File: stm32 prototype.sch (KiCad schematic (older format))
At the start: 98 parts, among them J1 Conn_01x04, J10 Conn_01x03, J12 Conn_01x07, J13 Conn_01x06, J2 Conn_02x05_Odd_Even, J3 Conn_01x08, J4 Conn_01x06, J5 Conn_01x06, J6 Conn_01x06, J7 Conn_01x06, J8 Conn_ARM_JTAG_SWD_10, J9 Conn_01x03, Q1 Q_NMOS_GSD, Q2 Q_NMOS_GSD, Q3 Q_NMOS_GSD, Q4 Q_NMOS_GSD, Q5 Q_NMOS_GSD, Q6 Q_NMOS_GSD, Q7 Q_NMOS_GSD, Q8 Q_NMOS_GSD, SW1 SW_Push, SW2 SW_Push, U1 STM32F405RGTx, U3 STM32F407VGTx, U7 TPS62203DBVR, Y1 Crystal_GND24, Y2 Crystal_GND24

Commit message: Worked on layout for new MCU
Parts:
- removed C10, C11, C39, C41, C5, C6, C7, C8, C9: .1uF, Capacitors_SMD:C_0603, symbol Device:C
- removed C16, C38: 2.2uF, Capacitors_SMD:C_0603, symbol Device:C
- removed C2, C3: 9pF, Capacitors_SMD:C_0603, symbol Device:C
- removed C4, C40: 1uF, Capacitors_SMD:C_0603, symbol Device:C
- removed D10, D11, D5, D6, D7, D8, D9: LED, LEDs:LED_1206, symbol Device:LED
- removed J1: Conn_01x04, Pin_Headers:Pin_Header_Straight_1x04_Pitch2.54mm, symbol Connector_Generic:Conn_01x04
- removed J12: Conn_01x07, Pin_Headers:Pin_Header_Straight_1x07_Pitch2.54mm, symbol Connector_Generic:Conn_01x07
- removed J13, J4, J5, J6, J7: Conn_01x06, Pin_Headers:Pin_Header_Straight_1x06_Pitch2.54mm, symbol Connector_Generic:Conn_01x06
- removed J3: Conn_01x08, Pin_Headers:Pin_Header_Straight_1x08_Pitch2.54mm, symbol Connector_Generic:Conn_01x08
- removed J8: Conn_ARM_JTAG_SWD_10, Pin_Headers:Pin_Header_Straight_2x05_Pitch1.27mm_SMD, symbol Connector:Conn_ARM_JTAG_SWD_10
- removed Q2, Q3, Q4, Q5, Q6, Q7, Q8: Q_NMOS_GSD, TO_SOT_Packages_SMD:SOT-323_SC-70, symbol Device:Q_NMOS_GSD
- removed R11, R13, R15, R17, R19, R21, R23, R47: 10K, Resistors_SMD:R_0603, symbol Device:R
- removed R12, R14, R16, R18, R20, R22, R24: 330R, Resistors_SMD:R_0603, symbol Device:R
- removed R31: 10k, Resistors_SMD:R_0603, symbol Device:R
- removed R46: DNP, Resistors_SMD:R_0603, symbol Device:R
- removed R48: 100K, Resistors_SMD:R_0603, symbol Device:R
- removed R52: 1MR, Resistors_SMD:R_0603, symbol Device:R
- removed SW1, SW2: SW_Push, switches_mdg:Switch_Tactile_6x6mm_Vertical_SMD_MJTP1230, symbol switches_mdg:SW_Push
- removed U3: STM32F407VGTx, Housings_QFP:LQFP-100_14x14mm_Pitch0.5mm, symbol MCU_ST_STM32F4:STM32F407VGTx
- removed Y1: Crystal_GND24, Crystals:Crystal_SMD_SeikoEpson_TSX3225-4pin_3.2x2.5mm, symbol Device:Crystal_GND24
- added J1, J8: Conn_01x25, Pin_Headers:Pin_Header_Straight_1x25_Pitch2.54mm, symbol Connector_Generic:Conn_01x25
- added SW1, SW2: SW_Push, switches_mdg:FSM2JMTR, symbol Switch:SW_Push
- C1, C12, C13, C14, C15, C17, C18, C19, C20, C21, C22, C23, C24, C42, C43: footprint Capacitors_SMD:C_0603 -> Capacitors_SMD:C_0603_HandSoldering
- J10, J9: footprint (none) -> Pin_Headers:Pin_Header_Straight_1x03_Pitch2.54mm
- J2: footprint Pin_Headers:Pin_Header_Straight_2x05_Pitch1.27mm_SMD -> Pin_Headers:Pin_Header_Straight_2x05_Pitch1.27mm; Part Number (none) -> FTSH-105-01-F-D-K
- L3: footprint Inductors_SMD:L_1210 -> Inductors_SMD:L_1210_HandSoldering
- Q1: footprint TO_SOT_Packages_SMD:SOT-323_SC-70 -> TO_SOT_Packages_SMD:SOT-323_SC-70_Handsoldering
- R1, R2, R3, R4, R5, R50, R51, R6, R7, R8: footprint Resistors_SMD:R_0603 -> Resistors_SMD:R_0603_HandSoldering
- R32: value 470R -> 10k; footprint Resistors_SMD:R_0603 -> Resistors_SMD:R_0603_HandSoldering
- U1: footprint Package_QFP:LQFP-64_10x10mm_P0.5mm -> Housings_QFP:LQFP-64_10x10mm_Pitch0.5mm
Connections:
- net labels added: PA0, PA10_ST_TXD, PA11_ST_RTS, PA12_CTS, PA15, PA3, PA4_SPI1_NSS, PA5_SPI1_SCK, PA6_SPI1_MISO, PA7_SPI1_MOSI, PA8_MCO, PA9_ST_RXD, PB3, PB5_I2C1_SMBA, PB6_I2C1_SCL, PB7_I2C1_SDA, PC10, PC11, PC12, PC15_STATUS, PC3, PC6, PC7, PC8, PC9
- net labels removed: FTDI_CTS, FTDI_DCD, FTDI_DCR, FTDI_RI, FTDI_ST_DTR, FTDI_ST_RTS, FTDI_ST_RXD, FTDI_ST_TXD, I2C1_SCL, I2C1_SDA, I2C1_SMBA, MEM_CHIP_SELECT, PB2, PC15, PD0, PD1, PD10, PD11, PD12, PD8, PD9, PE0, PE1, PE10, PE11, PE12, PE13, PE14, PE15, PE2, PE3, PE4, PE5, PE6, PE7, PE8, PE9, SPI1_MISO, SPI1_MOSI, SPI1_NSS, SPI1_SCK, SPI3_MISO, SPI3_MOSI, SPI3_NSS, SPI3_SCK, STATUS_BIT0, STATUS_BIT1, STATUS_BIT2, STATUS_BIT3, STATUS_BIT4, STATUS_BIT5, STATUS_BIT6, STATUS_BIT7, ST_HOLD, ST_WP, USART2_CK, USART2_CTS, USART2_RTS, USART2_RX, USART2_TX
- wire segments 330 -> 132
- no-connect marks 1 -> 2
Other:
- moved on the sheet: C12, C13, C14, C15, C17, C18, C19, C20, C21, C22, C23, C24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

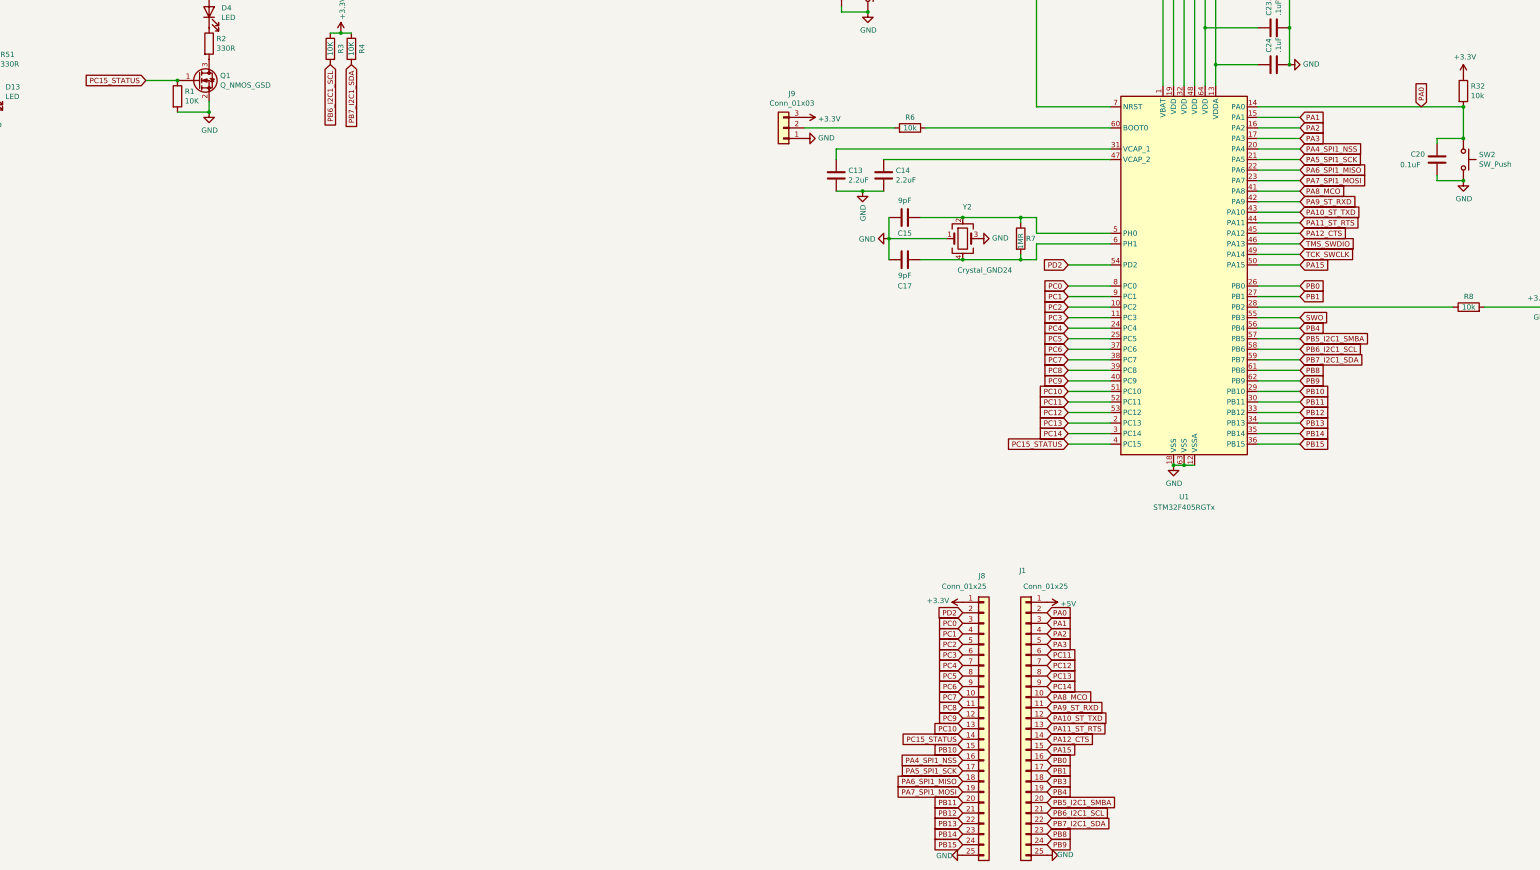
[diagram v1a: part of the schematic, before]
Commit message: finished layout, need to do final review before ordering PCB
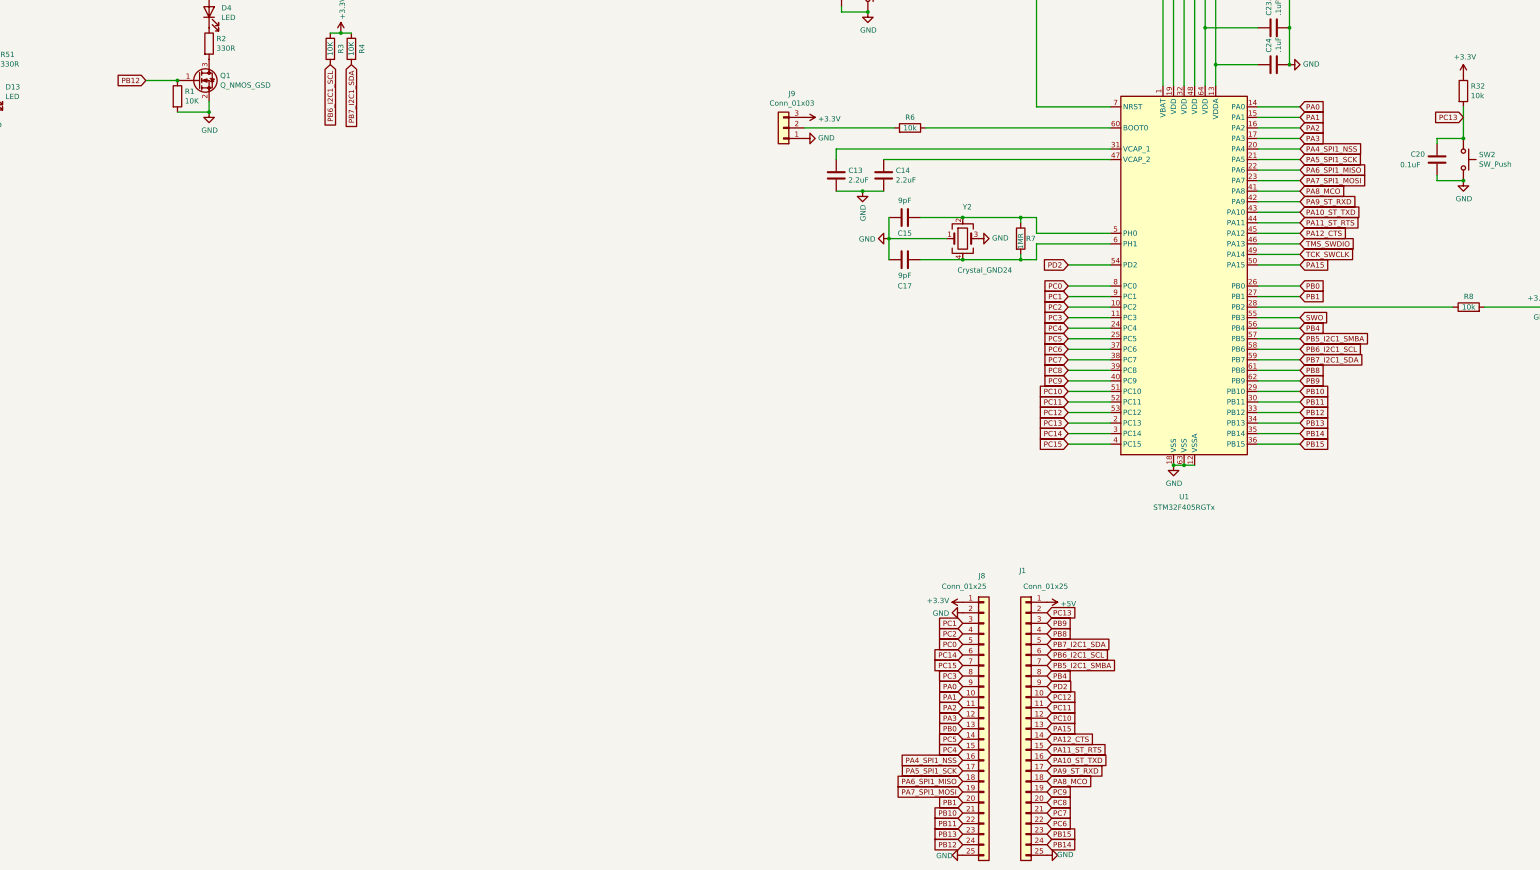
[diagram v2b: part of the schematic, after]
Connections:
- net PB3 is gone; now on net PA8_MCO: J1.18 (Pin_18)
- net GND: now also J8.2 (Pin_2)
- net PA0: now also J8.9 (Pin_9); no longer C20.2, J1.2 (Pin_2), R32.2, SW2.1
- net PA1: now also J8.10 (Pin_10); no longer J1.3 (Pin_3)
- net PA10_ST_TXD: now also J1.16 (Pin_16); no longer J1.12 (Pin_12)
- net PA11_ST_RTS: now also J1.15 (Pin_15); no longer J1.13 (Pin_13)
- net PA15: now also J1.13 (Pin_13); no longer J1.15 (Pin_15)
- net PA2: now also J8.11 (Pin_11); no longer J1.4 (Pin_4)
- net PA3: now also J8.12 (Pin_12); no longer J1.5 (Pin_5)
- net PA8_MCO: no longer J1.10 (Pin_10)
- net PA9_ST_RXD: now also J1.17 (Pin_17); no longer J1.11 (Pin_11)
- net PB0: now also J8.13 (Pin_13); no longer J1.16 (Pin_16)
- net PB1: now also J8.20 (Pin_20); no longer J1.17 (Pin_17)
- net PB10: now also J8.21 (Pin_21); no longer J8.15 (Pin_15)
- net PB11: now also J8.22 (Pin_22); no longer J8.20 (Pin_20)
- net PB12: now also J8.24 (Pin_24), Q1.1 (G), R1.1; no longer J8.21 (Pin_21)
- net PB13: now also J8.23 (Pin_23); no longer J8.22 (Pin_22)
- net PB14: now also J1.24 (Pin_24); no longer J8.23 (Pin_23)
- net PB15: now also J1.23 (Pin_23); no longer J8.24 (Pin_24)
- net PB4: now also J1.8 (Pin_8); no longer J1.19 (Pin_19)
- net PB5_I2C1_SMBA: now also J1.7 (Pin_7); no longer J1.20 (Pin_20)
- net PB6_I2C1_SCL: now also J1.6 (Pin_6); no longer J1.21 (Pin_21)
- net PB7_I2C1_SDA: now also J1.5 (Pin_5); no longer J1.22 (Pin_22)
- net PB8: now also J1.4 (Pin_4); no longer J1.23 (Pin_23)
- net PB9: now also J1.3 (Pin_3); no longer J1.24 (Pin_24)
- net PC0: now also J8.5 (Pin_5); no longer J8.3 (Pin_3)
- net PC1: now also J8.3 (Pin_3); no longer J8.4 (Pin_4)
- net PC10: now also J1.12 (Pin_12); no longer J8.13 (Pin_13)
- net PC11: now also J1.11 (Pin_11); no longer J1.6 (Pin_6)
- net PC12: now also J1.10 (Pin_10); no longer J1.7 (Pin_7)
- net PC13: now also C20.2, J1.2 (Pin_2), R32.2, SW2.1; no longer J1.8 (Pin_8)
- net PC14: now also J8.6 (Pin_6); no longer J1.9 (Pin_9)
- net PC2: now also J8.4 (Pin_4); no longer J8.5 (Pin_5)
- net PC3: now also J8.8 (Pin_8); no longer J8.6 (Pin_6)
- net PC4: now also J8.15 (Pin_15); no longer J8.7 (Pin_7)
- net PC5: now also J8.14 (Pin_14); no longer J8.8 (Pin_8)
- net PC6: now also J1.22 (Pin_22); no longer J8.9 (Pin_9)
- net PC7: now also J1.21 (Pin_21); no longer J8.10 (Pin_10)
- net PC8: now also J1.20 (Pin_20); no longer J8.11 (Pin_11)
- net PC9: now also J1.19 (Pin_19); no longer J8.12 (Pin_12)
- net PD2: now also J1.9 (Pin_9); no longer J8.2 (Pin_2)
- removed net PC15_STATUS: J8.14 (Pin_14), Q1.1 (G), R1.1, U1.4 (PC15)
- new net PC15: J8.7 (Pin_7), U1.4 (PC15)
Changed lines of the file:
@@
 	1    0    0    -1
 $EndComp
-Wire Wire Line
-	22000 7600 23950 7600
 $Comp
 L power:GND #PWR0133
@@
 NRST
 Text GLabel 20200 10800 0    50   Input ~ 0
-PC15_STATUS
+PC15
 NoConn ~ 16450 6400
 NoConn ~ 15950 6400
@@
 Wire Wire Line
 	20200 10800 20600 10800
-Text GLabel 20000 12400 2    50   Input ~ 0
+Text GLabel 19200 13100 0    50   Input ~ 0
 PA0
-Text GLabel 20000 13400 2    50   Input ~ 0
+Text GLabel 20000 13800 2    50   Input ~ 0
 PA10_ST_TXD
-Text GLabel 20000 13300 2    50   Input ~ 0
+Text GLabel 20000 13900 2    50   Input ~ 0
 PA9_ST_RXD
-Text GLabel 20000 13500 2    50   Input ~ 0
+Text GLabel 20000 13700 2    50   Input ~ 0
 PA11_ST_RTS
 Text GLabel 20000 13600 2    50   Input ~ 0
@@
 Text GLabel 19200 13800 0    50   Input ~ 0
 PA4_SPI1_NSS
+Text GLabel 19200 13200 0    50   Input ~ 0
+PA1
+Text GLabel 19200 13300 0    50   Input ~ 0
+PA2
+Text GLabel 19200 13400 0    50   Input ~ 0
+PA3
+Text GLabel 20000 14000 2    50   Input ~ 0
+PA8_MCO
+Text GLabel 20000 13500 2    50   Input ~ 0
+PA15
+Text GLabel 19200 13500 0    50   Input ~ 0
+PB0
+Text GLabel 19200 14200 0    50   Input ~ 0
+PB1
+Text GLabel 20000 12900 2    50   Input ~ 0
+PB5_I2C1_SMBA
+Text GLabel 20000 12700 2    50   Input ~ 0
+PB7_I2C1_SDA
+Text GLabel 20000 12800 2    50   Input ~ 0
+PB6_I2C1_SCL
+Text GLabel 20000 13000 2    50   Input ~ 0
+PB4
+Text GLabel 20000 12600 2    50   Input ~ 0
+PB8
 Text GLabel 20000 12500 2    50   Input ~ 0
-PA1
-Text GLabel 20000 12600 2    50   Input ~ 0
-PA2
-Text GLabel 20000 12700 2    50   Input ~ 0
-PA3
+PB9
+Text GLabel 19200 14300 0    50   Input ~ 0
+PB10
+Text GLabel 19200 14400 0    50   Input ~ 0
+PB11
+Text GLabel 19200 14600 0    50   Input ~ 0
+PB12
+Text GLabel 19200 14500 0    50   Input ~ 0
+PB13
+Text GLabel 20000 14600 2    50   Input ~ 0
+PB14
+Text GLabel 20000 14500 2    50   Input ~ 0
+PB15
+Text GLabel 19200 12900 0    50   Input ~ 0
+PC15
+Text GLabel 19200 12800 0    50   Input ~ 0
+PC14
+Text GLabel 20000 12400 2    50   Input ~ 0
+PC13
 Text GLabel 20000 13200 2    50   Input ~ 0
-PA8_MCO
-Text GLabel 20000 13700 2    50   Input ~ 0
-PA15
-Text GLabel 20000 13800 2    50   Input ~ 0
-PB0
-Text GLabel 20000 13900 2    50   Input ~ 0
-PB1
+PC12
+Text GLabel 20000 13300 2    50   Input ~ 0
+PC11
+Text GLabel 20000 13400 2    50   Input ~ 0
+PC10
+Text GLabel 20000 14100 2    50   Input ~ 0
+PC9
 Text GLabel 20000 14200 2    50   Input ~ 0
-PB5_I2C1_SMBA
+PC8
+Text GLabel 20000 14300 2    50   Input ~ 0
+PC7
 Text GLabel 20000 14400 2    50   Input ~ 0
-PB7_I2C1_SDA
-Text GLabel 20000 14300 2    50   Input ~ 0
-PB6_I2C1_SCL
-Text GLabel 20000 14000 2    50   Input ~ 0
-PB3
-Text GLabel 20000 14100 2    50   Input ~ 0
-PB4
-Text GLabel 20000 14500 2    50   Input ~ 0
-PB8
-Text GLabel 20000 14600 2    50   Input ~ 0
-PB9
+PC6
+Text GLabel 19200 13600 0    50   Input ~ 0
+PC5
 Text GLabel 19200 13700 0    50   Input ~ 0
-PB10
-Text GLabel 19200 14200 0    50   Input ~ 0
-PB11
-Text GLabel 19200 14300 0    50   Input ~ 0
-PB12
-Text GLabel 19200 14400 0    50   Input ~ 0
-PB13
-Text GLabel 19200 14500 0    50   Input ~ 0
-PB14
-Text GLabel 19200 14600 0    50   Input ~ 0
-PB15
-Text GLabel 19200 13600 0    50   Input ~ 0
-PC15_STATUS
+PC4
+Text GLabel 19200 13000 0    50   Input ~ 0
+PC3
+Text GLabel 19200 12600 0    50   Input ~ 0
+PC2
+Text GLabel 19200 12500 0    50   Input ~ 0
+PC1
+Text GLabel 19200 12700 0    50   Input ~ 0
+PC0
 Text GLabel 20000 13100 2    50   Input ~ 0
-PC14
-Text GLabel 20000 13000 2    50   Input ~ 0
-PC13
-Text GLabel 20000 12900 2    50   Input ~ 0
-PC12
-Text GLabel 20000 12800 2    50   Input ~ 0
-PC11
-Text GLabel 19200 13500 0    50   Input ~ 0
-PC10
-Text GLabel 19200 13400 0    50   Input ~ 0
-PC9
-Text GLabel 19200 13300 0    50   Input ~ 0
-PC8
-Text GLabel 19200 13200 0    50   Input ~ 0
-PC7
-Text GLabel 19200 13100 0    50   Input ~ 0
-PC6
-Text GLabel 19200 13000 0    50   Input ~ 0
-PC5
-Text GLabel 19200 12900 0    50   Input ~ 0
-PC4
-Text GLabel 19200 12800 0    50   Input ~ 0
-PC3
-Text GLabel 19200 12700 0    50   Input ~ 0
-PC2
-Text GLabel 19200 12600 0    50   Input ~ 0
-PC1
-Text GLabel 19200 12500 0    50   Input ~ 0
-PC0
-Text GLabel 19200 12400 0    50   Input ~ 0
 PD2
 $Comp
@@
 Connection ~ 23950 7900
 Connection ~ 23950 8300
-Connection ~ 23950 7600
-Text GLabel 11450 7350 0    50   Input ~ 0
-PC15_STATUS
 Wire Wire Line
 	23950 7600 23950 7900
-Text GLabel 23550 7600 1    50   Input ~ 0
+Text GLabel 22400 7600 2    50   Input ~ 0
 PA0
 Connection ~ 13300 6900
 Wire Wire Line
 	13300 6900 13400 6900
+Text GLabel 11450 7350 0    50   Input ~ 0
+PB12
+Text GLabel 23950 7700 0    50   Input ~ 0
+PC13
+Wire Wire Line
+	22000 7600 22400 7600
+$Comp
+L power:GND #PWR0105
+U 1 1 5C31B366
+P 19200 12400
+F 0 "#PWR0105" H 19200 12150 50  0001 C CNN
+F 1 "GND" V 19205 12272 50  0000 R CNN
+F 2 "" H 19200 12400 50  0001 C CNN
+F 3 "" H 19200 12400 50  0001 C CNN
+	1    19200 12400
+	0    1    1    0
+$EndComp
 $EndSCHEMATC
